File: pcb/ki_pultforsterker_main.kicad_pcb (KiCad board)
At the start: 2 copper layers, 180 x 100 mm, 264 parts, among them J1 24V IN, J10 LED-RINGER, J11 PC1, J12 PC2, J13 TFT, J15 USB1, J16 USB2, J17 USB3, J18 USB4, J19 USB PI, J2 SPK L, J20 AUX2, J21 PWR BAK, J22 EXP, J23 HODETLF, J24 NTC, J3 SPK R, J4 AUX1, J5 RPi 40-pin, J6 5V -> PI, J7 KNAPPER, J8 ENCODER, J9 OLED, K1 SRD-05VDC-SL-C, Q10 AO3401A, Q11 P-MOSFET 60V 20A (AOD409), Q2 AO3400A, Q3 AO3400A, Q4 AO3400A, Q5 AO3400A, Q6 AO3400A, Q7 AO3400A, Q8 AO3401A, Q9 AO3400A, U1 TPS54560DDAR, U10 PCM1808PWR, U11 PCM2900CDB, U12 MCP23017-E/SS, U13 TPA6132A2RTER, U14 74LVC1G14, U2 AMS1117-3.3, U3 LM2662MX, U4 PCM5102APWR, U5 PGA2311UA, U6 TPA3116D2DADR, U7 FE1.1s, U8 TS3USB221RSER, U9 AMS1117-3.3, X1 12.288MHz, Y1 12MHz, Y2 12MHz

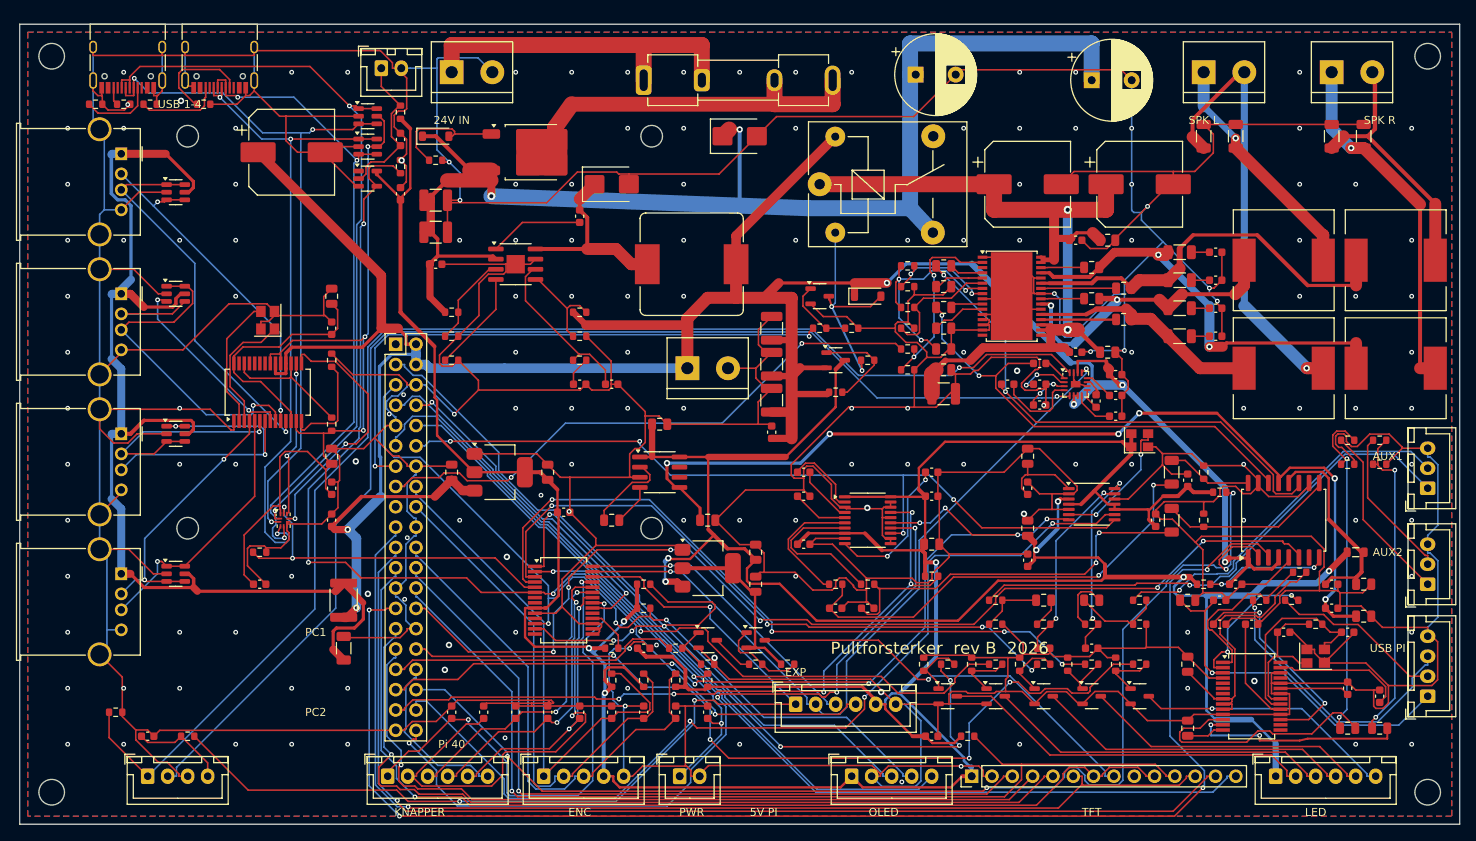
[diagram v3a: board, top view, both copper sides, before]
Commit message: PCB rev B: produksjonsfiler etter granskning – DRC uten klarings-, hull-, kant- eller koblingsfeil; BOM/CPL med verifiserte koder, JLCPCB-rotasjoner, THT i egen liste
Co-Authored-By: Claude Fable 5.1 <noreply@anthropic.com>
Claude-Session: https://claude.ai/code/session_01FaJKmYinw8SWRobKXBRYpt
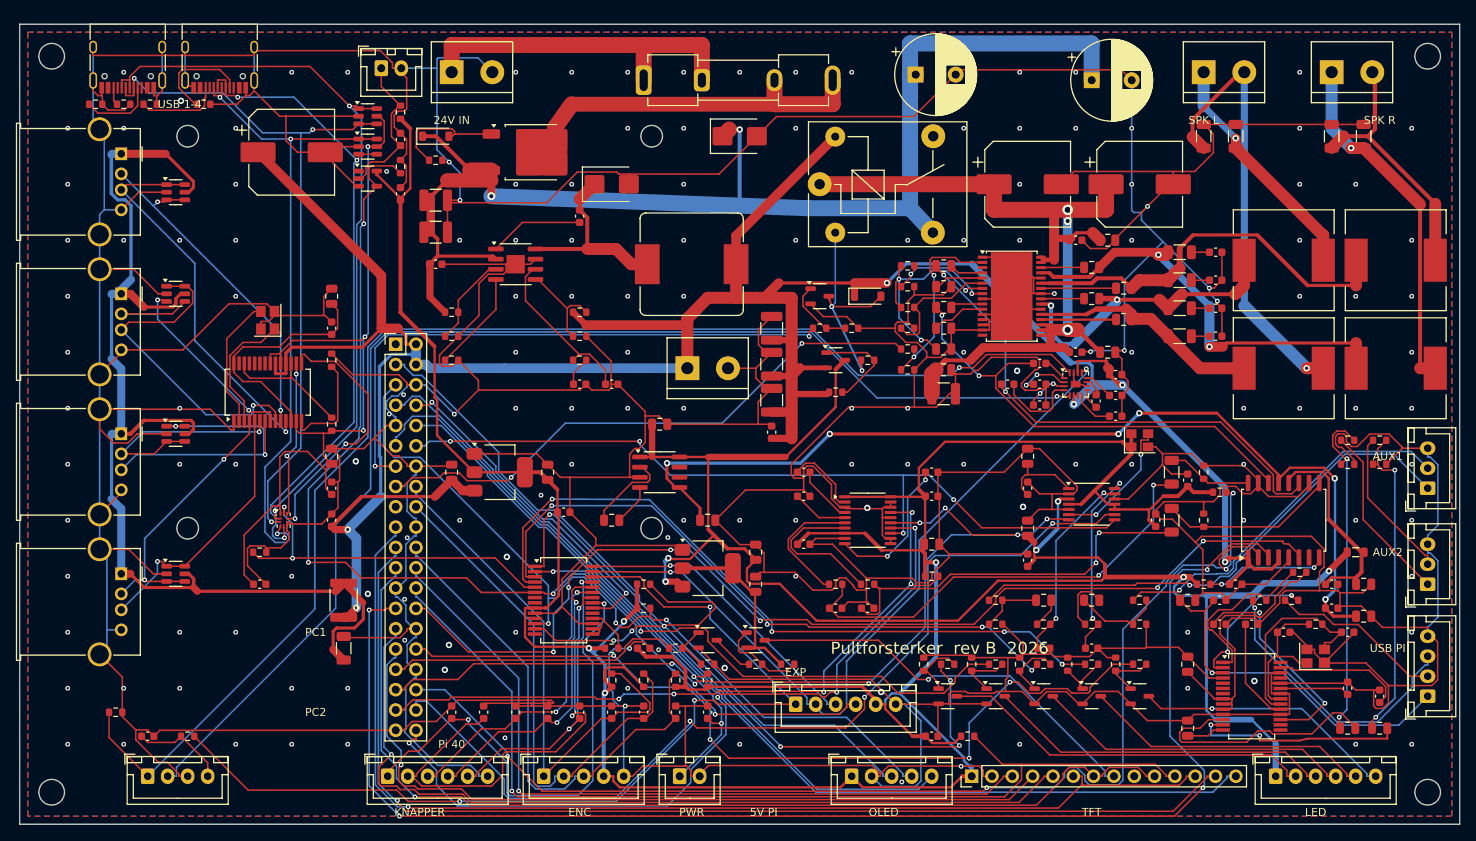
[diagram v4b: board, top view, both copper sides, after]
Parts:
- C10, C8, C9: value 47u/10V -> 47u/16V
- C23, C24: value 2.2n -> 2.2n/50V
- C40, C41, C72: value 220u/35V -> 220u/50V
- C87, C88: value 20p -> 22p
- D2: value SS56 -> SS56 (SMB)
- F1: value 5A 5x20 -> 5A 5x20 (Keystone 3512-klips)
- L1: value 10uH 6A -> 10uH 6A SRP1245A-100M
- L2, L3, L4, L5: value 10uH 7A -> 10uH 4A
- R17: value 0 -> 0R
- R2: value 51k -> 49.9k
- R21, R22, R23, R24: value 18 -> 18R 1206
- R5: value 10.2k -> 10k
- R6: value 13.3k -> 13k
- R64, R65: value 22 -> 22R
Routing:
- net GND: track 1815.2 -> 1805.4 mm, vias 157 -> 156
- net 24V_AMP: vias 2 -> 3

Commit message: PCB sluttkontroll: J6 bort fra Pi-ens USB3-blokk, VIN24 dobbel/større via, 24V_AMP-skinne forlenget, L1 = C2042471, rapport og sjekkliste oppdatert
Co-Authored-By: Claude Fable 5.1 <noreply@anthropic.com>
Claude-Session: https://claude.ai/code/session_01FaJKmYinw8SWRobKXBRYpt
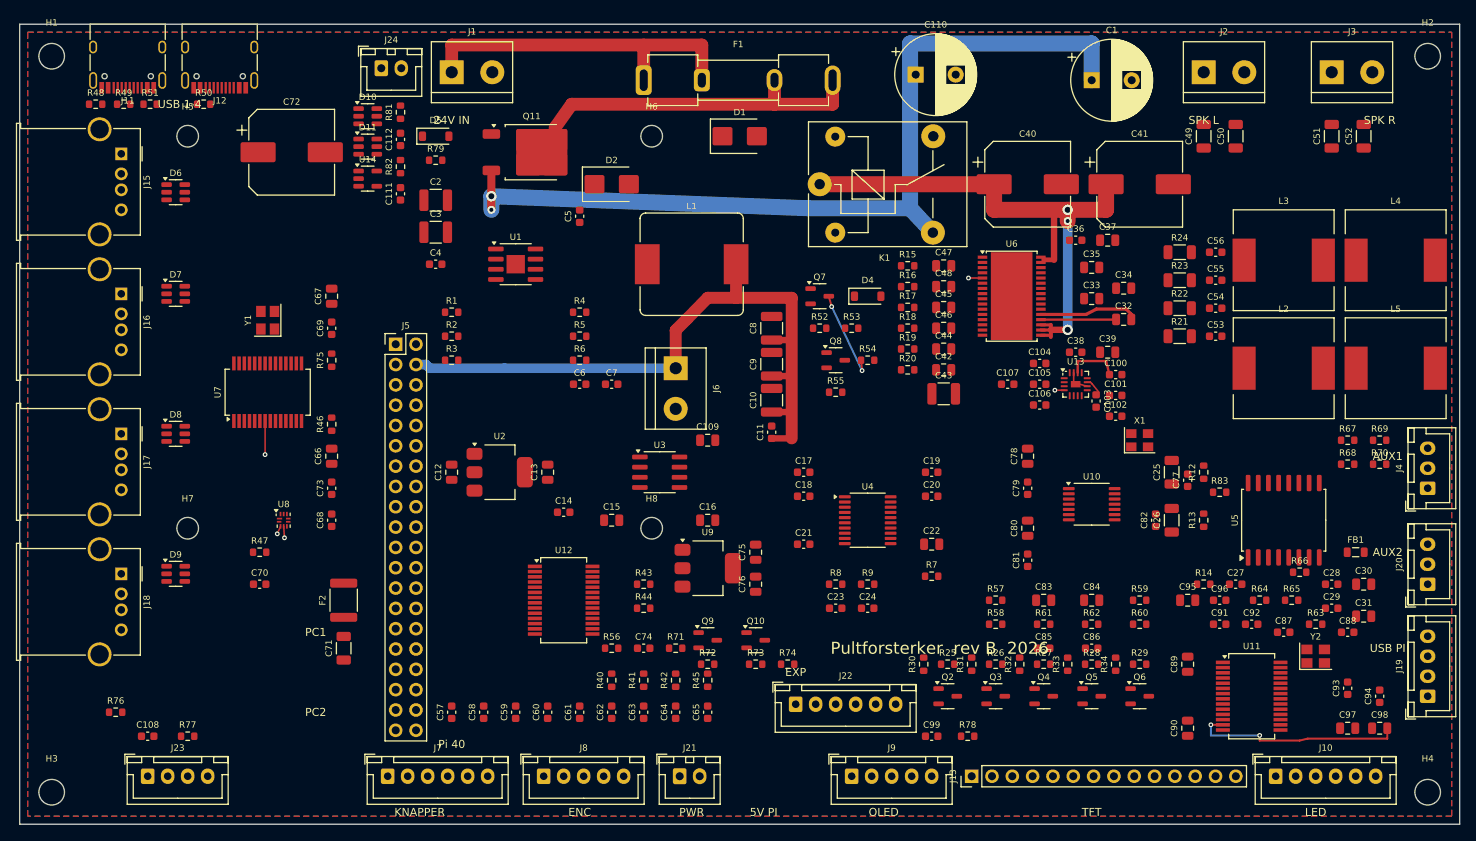
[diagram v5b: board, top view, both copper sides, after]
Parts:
- R4: value 56k -> 33k
- R5: value 10k -> 6.2k
- moved C109 6.32 mm to (86.0, 52.0)
- moved J6 1.46 mm to (82.0, 43.0), turned to -90 degrees
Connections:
- C109 pad 1: 5V_SW -> 5V
- FB1 pad 1: 5V_SW -> 5V
- J11 pad : (no net) -> GND
- J12 pad : (no net) -> GND
- R14 pad 1: 5V_SW -> 5V
- U1 pad : (no net) -> GND
- U13 pad : (no net) -> GND
- U3 pad 1: 5V_SW -> 5V
- U3 pad 8: 5V_SW -> 5V
- U6 pad : (no net) -> GND
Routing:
- net GND: track 1805.4 -> 2.11 mm, vias 156 -> 0
- net 3V3: track 373.0 -> 0.00 mm, vias 4 -> 0
- net 5V: track 360.0 -> 92.1 mm, vias 6 -> 0
- net 5V_SW: track 210.1 -> 0.00 mm, vias 6 -> 0
- net PGA_SDI: track 175.5 -> 0.00 mm, vias 4 -> 0
- net HP_OUTL: track 168.1 -> 0.00 mm, vias 1 -> 0
- net HP_OUTR: track 156.4 -> 0.00 mm, vias 1 -> 0
- net PGA_CS: track 151.5 -> 0.00 mm, vias 4 -> 0
- net SPI_MOSI: track 141.0 -> 0.00 mm, vias 1 -> 0
- net 5V_USB: track 139.2 -> 0.00 mm
- net SPI_MISO: track 138.7 -> 0.00 mm, vias 1 -> 0
- net EXP_B5: track 137.7 -> 0.00 mm, vias 4 -> 0
- net PGA_SCLK: track 132.0 -> 0.00 mm, vias 6 -> 0
- net TOUCH_IRQ: track 128.5 -> 0.00 mm
- net SPI_SCLK: track 128.0 -> 0.00 mm, vias 1 -> 0
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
